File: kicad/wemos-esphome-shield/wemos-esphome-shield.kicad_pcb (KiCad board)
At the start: 2 copper layers, 74 x 52 mm, 28 parts, among them Q1 2N2219, Q2 2N2219, Q3 2N2219, T1 Transformer_1P_1S, U1 WeMos_D1_mini

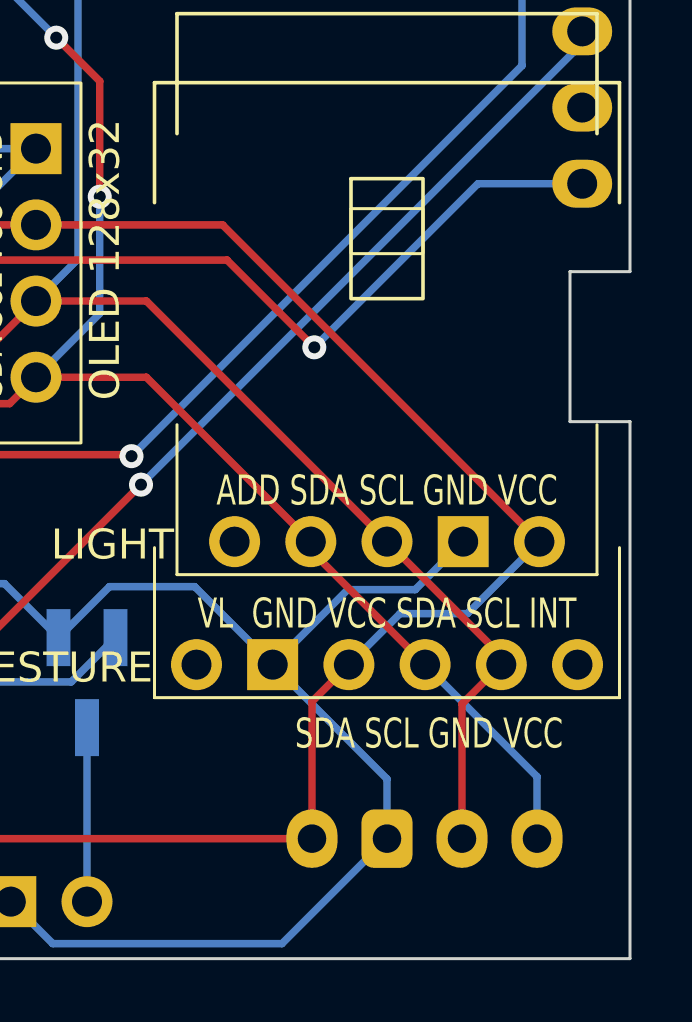
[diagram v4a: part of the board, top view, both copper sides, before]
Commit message: route gesture sensor to 3.3v power
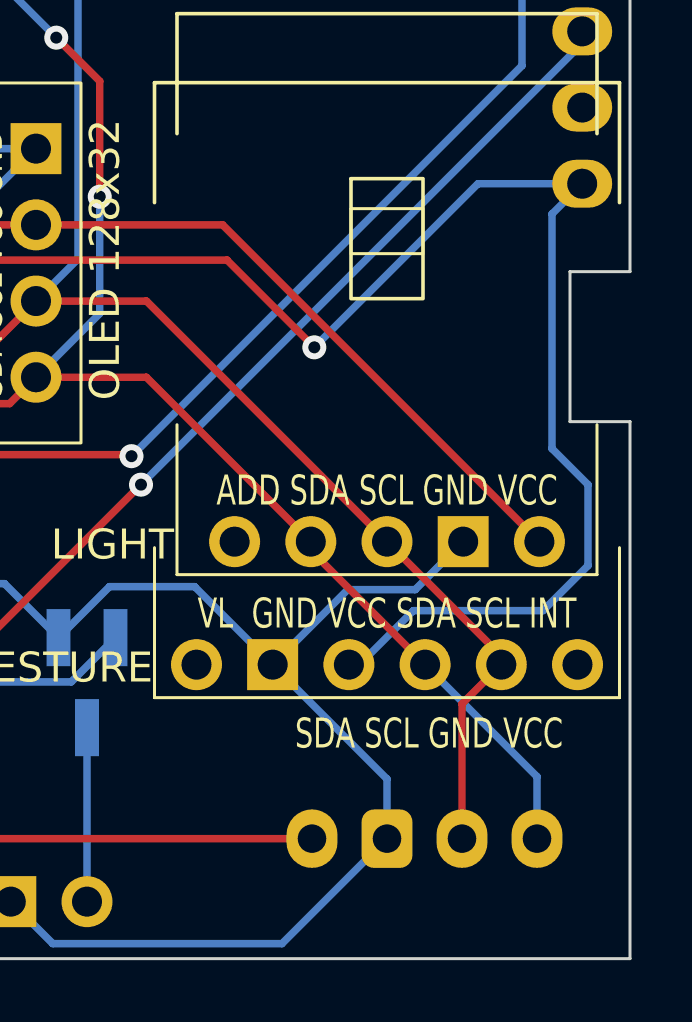
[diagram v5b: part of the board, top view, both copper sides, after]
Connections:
- GEST1 pad 3: 5V -> 3.3V
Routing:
- net 3.3V: track 79.0 -> 102.0 mm
- net 5V: track 219.6 -> 205.2 mm
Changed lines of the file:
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@@
       (net 6 "GND") (pinfunction "Pin_2") (pintype "passive"))
     (pad "3" thru_hole circle (at -1.27 0) (size 1.7 1.7) (drill 1) (layers "*.Cu" "*.Mask")
-      (net 1 "5V") (pinfunction "Pin_3") (pintype "passive"))
+      (net 5 "3.3V") (pinfunction "Pin_3") (pintype "passive"))
     (pad "4" thru_hole circle (at 1.27 0) (size 1.7 1.7) (drill 1) (layers "*.Cu" "*.Mask")
       (net 2 "SDA") (pinfunction "Pin_4") (pintype "passive"))
@@
   (segment (start 149.98 102.1) (end 139.42 91.54) (width 0.25) (layer "F.Cu") (net 1))
   (segment (start 117.17 101.4) (end 117.17 99.93) (width 0.25) (layer "F.Cu") (net 1))
-  (segment (start 142.4 112) (end 142.4 107.43) (width 0.25) (layer "F.Cu") (net 1))
   (segment (start 123.724 109.828) (end 107.924 109.828) (width 0.25) (layer "F.Cu") (net 1))
   (segment (start 123.724 109.828) (end 125.548 109.828) (width 0.25) (layer "F.Cu") (net 1))
@@
   (segment (start 112.7 88.2) (end 108.9 92) (width 0.25) (layer "F.Cu") (net 1))
   (segment (start 125.548 109.828) (end 129.82 114.1) (width 0.25) (layer "F.Cu") (net 1))
-  (segment (start 142.4 107.43) (end 143.63 106.2) (width 0.25) (layer "F.Cu") (net 1))
   (segment (start 83.712 104.748) (end 96.46 92) (width 0.25) (layer "F.Cu") (net 1))
   (segment (start 99.56 95.1) (end 123.4 95.1) (width 0.25) (layer "F.Cu") (net 1))
   (via (at 121 75.8) (size 0.8) (drill 0.4) (layers "F.Cu" "B.Cu") (net 1))
-  (segment (start 143.63 106.2) (end 145.33 104.5) (width 0.25) (layer "B.Cu") (net 1))
-  (segment (start 145.33 104.5) (end 147.58 104.5) (width 0.25) (layer "B.Cu") (net 1))
   (segment (start 121 72.51) (end 121 75.8) (width 0.25) (layer "B.Cu") (net 1))
-  (segment (start 147.58 104.5) (end 149.98 102.1) (width 0.25) (layer "B.Cu") (net 1))
   (segment (start 146.17 106.2) (end 142.36 102.39) (width 0.25) (layer "F.Cu") (net 2))
   (segment (start 80.838 112.368) (end 84 109.206) (width 0.25) (layer "F.Cu") (net 2))
@@
   (via (at 127.7 92.7) (size 0.8) (drill 0.4) (layers "F.Cu" "B.Cu") (net 5))
   (via (at 142.477347 95.622653) (size 0.8) (drill 0.4) (layers "F.Cu" "B.Cu") (net 5))
+  (segment (start 150.4 99) (end 150.4 91.177) (width 0.25) (layer "B.Cu") (net 5))
   (segment (start 112.732653 97.517347) (end 83.782653 97.517347) (width 0.25) (layer "B.Cu") (net 5))
   (segment (start 83.782653 97.517347) (end 80.838 100.462) (width 0.25) (layer "B.Cu") (net 5))
   (segment (start 127.7 92.7) (end 117.55 92.7) (width 0.25) (layer "B.Cu") (net 5))
   (segment (start 142.477347 95.622653) (end 147.93 90.17) (width 0.25) (layer "B.Cu") (net 5))
+  (segment (start 151.6 100.2) (end 150.4 99) (width 0.25) (layer "B.Cu") (net 5))
+  (segment (start 151.6 102.9) (end 151.6 100.2) (width 0.25) (layer "B.Cu") (net 5))
+  (segment (start 145.776396 104.4) (end 150.1 104.4) (width 0.25) (layer "B.Cu") (net 5))
   (segment (start 117.55 92.7) (end 112.732653 97.517347) (width 0.25) (layer "B.Cu") (net 5))
   (segment (start 80.838 100.462) (end 80.838 102.208) (width 0.25) (layer "B.Cu") (net 5))
+  (segment (start 150.4 91.177) (end 151.407 90.17) (width 0.25) (layer "B.Cu") (net 5))
+  (segment (start 150.1 104.4) (end 151.6 102.9) (width 0.25) (layer "B.Cu") (net 5))
+  (segment (start 143.63 106.2) (end 143.976396 106.2) (width 0.25) (layer "B.Cu") (net 5))
   (segment (start 147.93 90.17) (end 151.407 90.17) (width 0.25) (layer "B.Cu") (net 5))
+  (segment (start 143.976396 106.2) (end 145.776396 104.4) (width 0.25) (layer "B.Cu") (net 5))
   (segment (start 123.724 114.908) (end 126.132 112.5) (width 0.25) (layer "B.Cu") (net 6))
   (segment (start 129.75 103.5) (end 128.15 105.1) (width 0.25) (layer "B.Cu") (net 6))

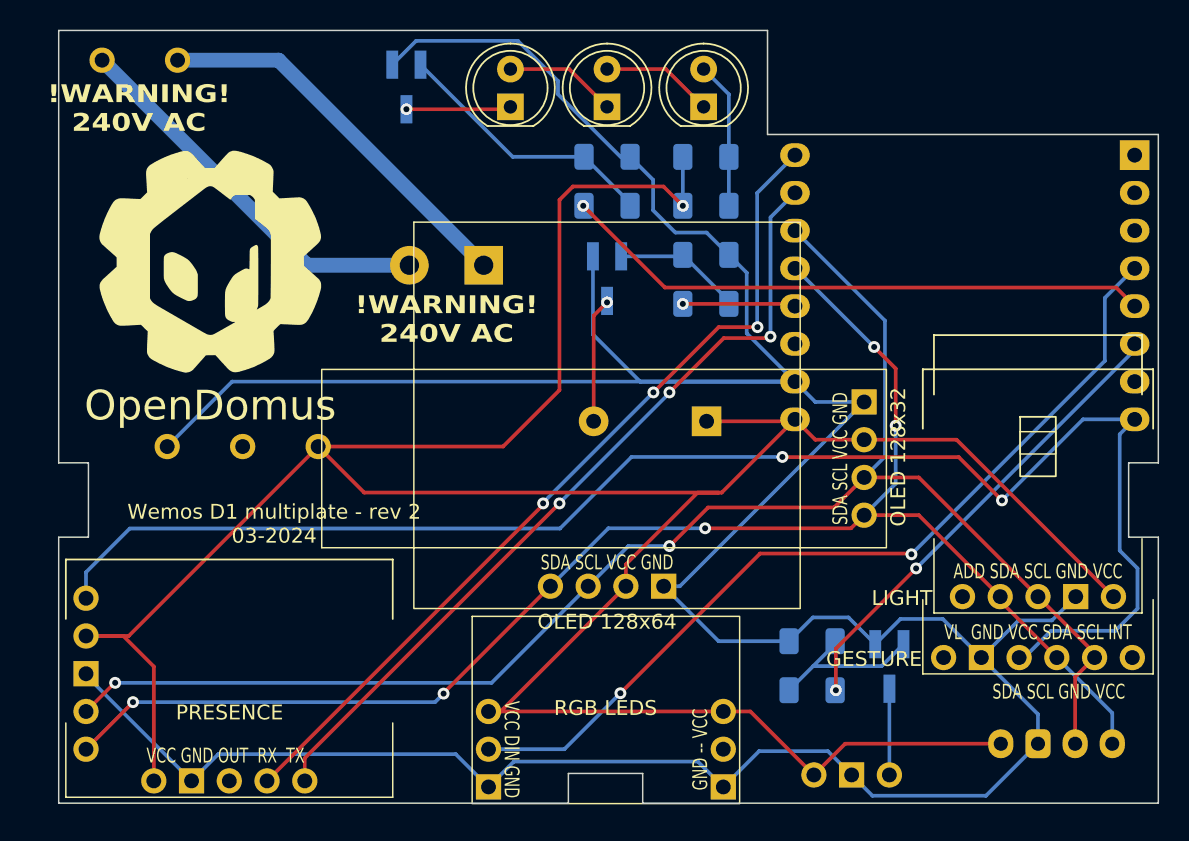
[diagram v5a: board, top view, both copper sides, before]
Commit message: custom SOT-23 footprint and other small adjustments
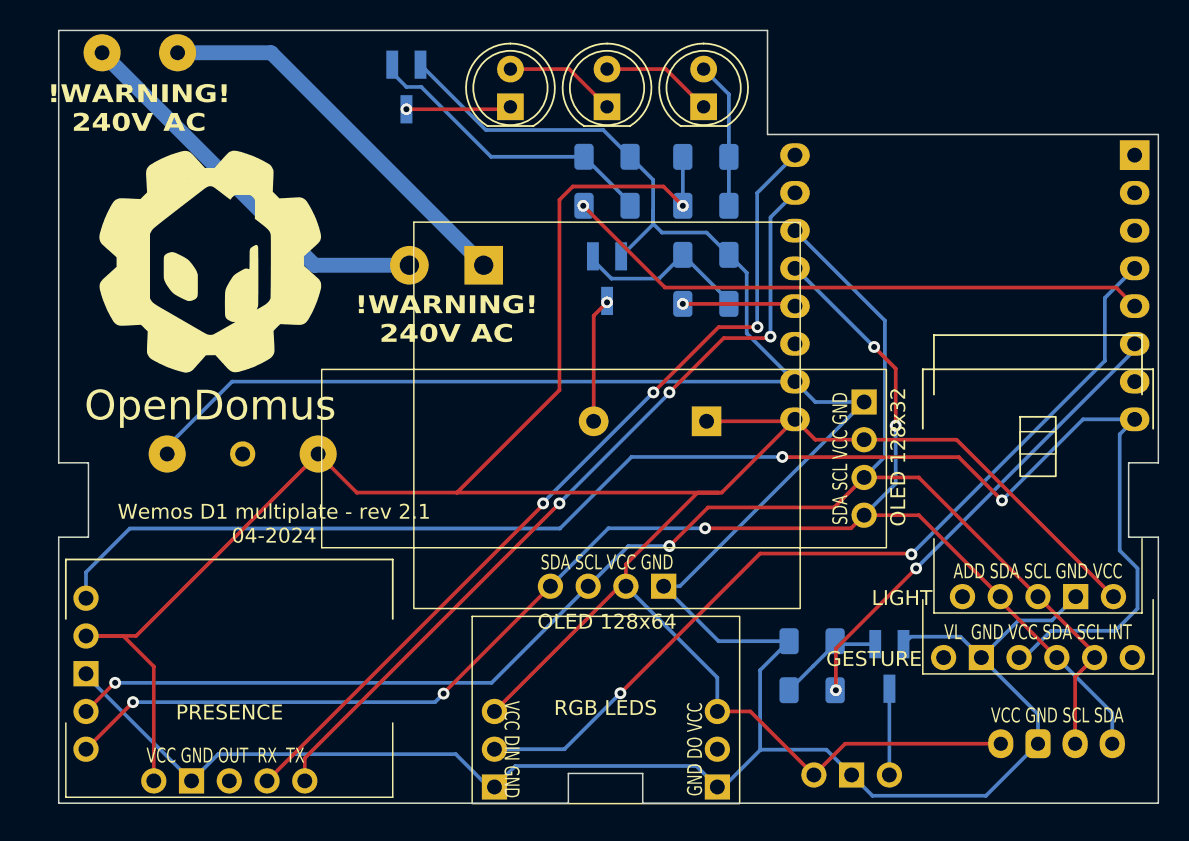
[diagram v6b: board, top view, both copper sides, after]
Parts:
- Q1, Q2, Q3: value 2N2219 -> 2N2222; footprint Package_TO_SOT_SMD:SOT-23_Handsoldering -> internal:SOT-23_Handsoldering
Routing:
- net GND: track 244.8 -> 222.9 mm
- net 5V: track 205.2 -> 192.7 mm
- net Net-(Q2-B): track 11.3 -> 7.37 mm
- net Net-(Q1-B): track 8.78 -> 12.1 mm
- net Net-(Q3-B): track 18.2 -> 20.4 mm
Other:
- board text added: "VCC GND SCL SDA"
- board text added: "Wemos D1 multiplate - rev 2.1 04-2024"
- board text removed: "SDA SCL GND VCC"
- board text removed: "Wemos D1 multiplate - rev 2 03-2024"

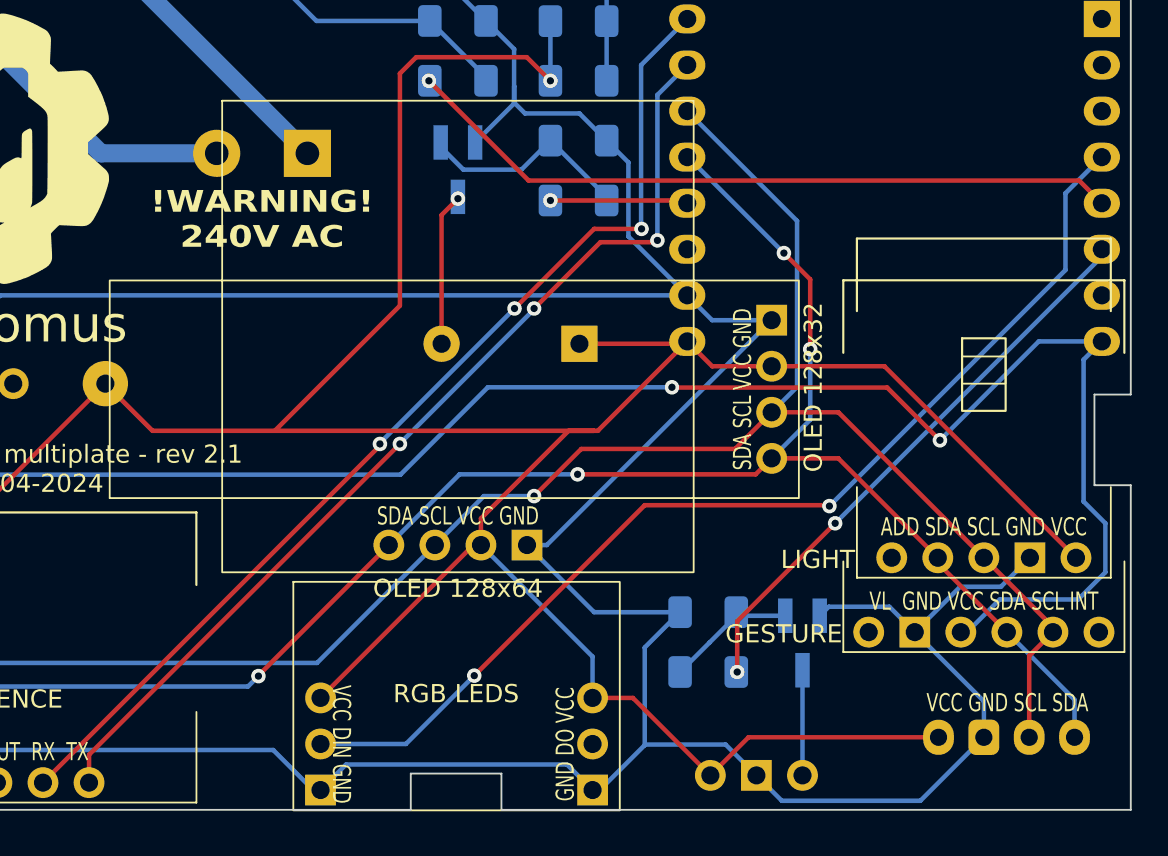
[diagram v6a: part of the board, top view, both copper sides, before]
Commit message: center oled display
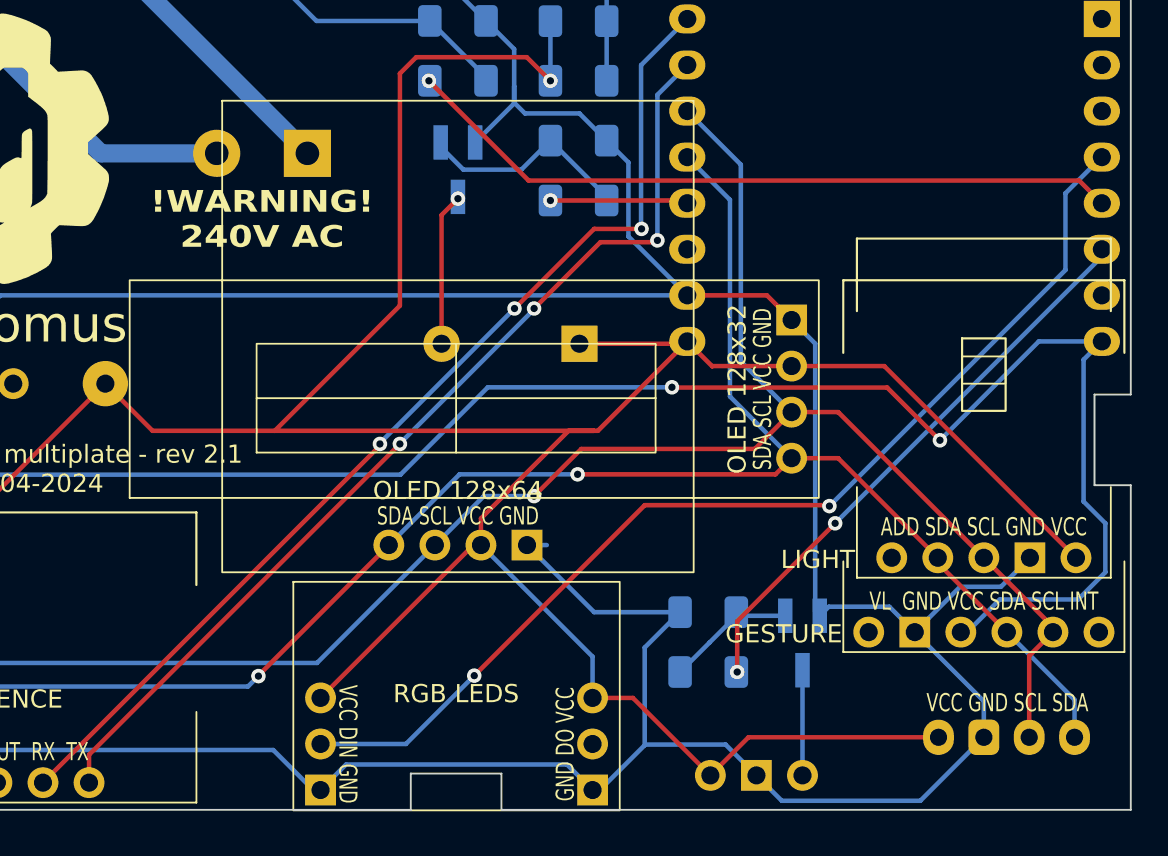
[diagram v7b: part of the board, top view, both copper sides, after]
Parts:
- moved OLED1 1.10 mm to (134.3, 92.8)
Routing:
- net SDA: track 103.7 -> 102.4 mm, vias 5 -> 3
- net SCL: track 105.6 -> 104.9 mm
- net GND: track 222.9 -> 223.4 mm

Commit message: reroute buzzer to D8
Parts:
- turned R1 to 180 degrees
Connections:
- R1 pad 1: D3 -> D8
- U1 pad 12: D3 -> unconnected-(U1-D3-Pad12)
- U1 pad 7: unconnected-(U1-CS/D8-Pad7) -> D8
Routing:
- net D8: track 0.00 -> 29.7 mm, vias 0 -> 1
- net D3: track 7.61 -> 0.00 mm, vias 1 -> 0
- net Net-(Q1-B): track 12.1 -> 10.8 mm
- net GND: track 223.4 -> 222.3 mm
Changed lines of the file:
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@@
   (net 7 "Net-(BZ1--)")
   (net 8 "D5")
-  (net 9 "D3")
+  (net 9 "D8")
   (net 10 "L")
   (net 11 "N")
@@
   (net 29 "unconnected-(U1-A0-Pad2)")
   (net 30 "unconnected-(U1-D0-Pad3)")
-  (net 31 "unconnected-(U1-CS{slash}D8-Pad7)")
+  (net 31 "unconnected-(U1-D3-Pad12)")
   (net 32 "unconnected-(U1-D4-Pad11)")
   (footprint "LED_THT:LED_D5.0mm" (layer "F.Cu")
@@
   )
   (footprint "Resistor_SMD:R_1206_3216Metric_Pad1.30x1.75mm_HandSolder" (layer "B.Cu")
-    (at 122.55 82.4)
+    (at 122.55 82.4 180)
     (descr "Resistor SMD 1206 (3216 Metric), square (rectangular) end terminal, IPC_7351 nominal with elongated pad for handsoldering. (Body size source: IPC-SM-782 page 72, https://www.pcb-3d.com/wordpress/wp-content/uploads/ipc-sm-782a_amendment_1_and_2.pdf), generated with kicad-footprint-generator")
     (tags "resistor handsolder")
@@
     (fp_line (start 1.6 0.8) (end 1.6 -0.8)
       (stroke (width 0.1) (type solid)) (layer "B.Fab"))
-    (pad "1" smd roundrect (at -1.55 0) (size 1.3 1.75) (layers "B.Cu" "B.Paste" "B.Mask") (roundrect_rratio 0.1923076923)
-      (net 9 "D3") (pintype "passive"))
-    (pad "2" smd roundrect (at 1.55 0) (size 1.3 1.75) (layers "B.Cu" "B.Paste" "B.Mask") (roundrect_rratio 0.1923076923)
+    (pad "1" smd roundrect (at -1.55 0 180) (size 1.3 1.75) (layers "B.Cu" "B.Paste" "B.Mask") (roundrect_rratio 0.1923076923)
+      (net 9 "D8") (pintype "passive"))
+    (pad "2" smd roundrect (at 1.55 0 180) (size 1.3 1.75) (layers "B.Cu" "B.Paste" "B.Mask") (roundrect_rratio 0.1923076923)
       (net 24 "Net-(Q1-B)") (pintype "passive"))
     (model "${KICAD6_3DMODEL_DIR}/Resistor_SMD.3dshapes/R_1206_3216Metric.wrl"
@@
       (net 12 "D7") (pinfunction "MOSI/D7") (pintype "bidirectional"))
     (pad "7" thru_hole oval (at 0 -15.24 180) (size 2 1.6) (drill 1) (layers "*.Cu" "*.Mask")
-      (net 31 "unconnected-(U1-CS{slash}D8-Pad7)") (pinfunction "CS/D8") (pintype "bidirectional+no_connect"))
+      (net 9 "D8") (pinfunction "CS/D8") (pintype "bidirectional"))
     (pad "8" thru_hole oval (at 0 -17.78 180) (size 2 1.6) (drill 1) (layers "*.Cu" "*.Mask")
       (net 5 "3.3V") (pinfunction "3V3") (pintype "power_out"))
@@
       (net 32 "unconnected-(U1-D4-Pad11)") (pinfunction "D4") (pintype "bidirectional+no_connect"))
     (pad "12" thru_hole oval (at 22.86 -10.16 180) (size 2 1.6) (drill 1) (layers "*.Cu" "*.Mask")
-      (net 9 "D3") (pinfunction "D3") (pintype "bidirectional"))
+      (net 31 "unconnected-(U1-D3-Pad12)") (pinfunction "D3") (pintype "bidirectional+no_connect"))
     (pad "13" thru_hole oval (at 22.86 -7.62 180) (size 2 1.6) (drill 1) (layers "*.Cu" "*.Mask")
       (net 2 "SDA") (pinfunction "SDA/D2") (pintype "bidirectional"))
@@
   (segment (start 130.66 112.4) (end 126.232 112.4) (width 0.25) (layer "B.Cu") (net 6))
   (segment (start 119 77) (end 119.6 77.6) (width 0.25) (layer "B.Cu") (net 6))
-  (segment (start 119.71 101.4) (end 120.8 101.4) (width 0.25) (layer "B.Cu") (net 6))
   (segment (start 126.232 112.4) (end 126.2 112.432) (width 0.25) (layer "B.Cu") (net 6))
   (segment (start 135.85 105.3) (end 136.35 104.8) (width 0.25) (layer "B.Cu") (net 6))
@@
   (segment (start 151.39 80.01) (end 151.407 80.01) (width 0.25) (layer "B.Cu") (net 8))
   (segment (start 149.4 86.235087) (end 149.4 82) (width 0.25) (layer "B.Cu") (net 8))
-  (segment (start 121 82.4) (end 128.397 82.4) (width 0.25) (layer "F.Cu") (net 9))
-  (segment (start 128.397 82.4) (end 128.547 82.55) (width 0.25) (layer "F.Cu") (net 9))
-  (via (at 121 82.4) (size 0.8) (drill 0.4) (layers "F.Cu" "B.Cu") (net 9))
+  (segment (start 124.1 82.4) (end 126.2 82.4) (width 0.25) (layer "F.Cu") (net 9))
+  (segment (start 126.2 82.4) (end 127.6 83.8) (width 0.25) (layer "F.Cu") (net 9))
+  (segment (start 127.6 83.8) (end 147.577 83.8) (width 0.25) (layer "F.Cu") (net 9))
+  (segment (start 147.577 83.8) (end 151.407 87.63) (width 0.25) (layer "F.Cu") (net 9))
+  (via (at 124.1 82.4) (size 0.8) (drill 0.4) (layers "F.Cu" "B.Cu") (net 9))
+  (segment (start 124.1 82.4) (end 124.1 82.2) (width 0.25) (layer "B.Cu") (net 9))
   (segment (start 96.22 79.8) (end 102.6 79.8) (width 1) (layer "B.Cu") (net 10))
   (segment (start 81.92 65.5) (end 96.22 79.8) (width 1) (layer "B.Cu") (net 10))
@@
   (segment (start 114.95 79.45) (end 116.2 80.7) (width 0.25) (layer "B.Cu") (net 24))
   (segment (start 119.4 80.7) (end 121 79.1) (width 0.25) (layer "B.Cu") (net 24))
-  (segment (start 124.1 82.2) (end 121 79.1) (width 0.25) (layer "B.Cu") (net 24))
   (segment (start 114.95 79.2) (end 114.95 79.45) (width 0.25) (layer "B.Cu") (net 24))
+  (segment (start 121 79.1) (end 121 82.4) (width 0.25) (layer "B.Cu") (net 24))
   (segment (start 116.2 80.7) (end 119.4 80.7) (width 0.25) (layer "B.Cu") (net 24))
-  (segment (start 124.1 82.4) (end 124.1 82.2) (width 0.25) (layer "B.Cu") (net 24))
   (segment (start 129.775 106.775) (end 128.15 108.4) (width 0.25) (layer "B.Cu") (net 25))
   (segment (start 131.45 105.3) (end 131.25 105.1) (width 0.25) (layer "B.Cu") (net 25))
@@
   (segment (start 108.1 72.5) (end 114.35 72.5) (width 0.25) (layer "B.Cu") (net 27))
   (segment (start 102.4 67.8) (end 103.4 67.8) (width 0.25) (layer "B.Cu") (net 27))
+  (segment (start 128.397 82.4) (end 128.547 82.55) (width 0.25) (layer "F.Cu") (net 31))
   (group "" (id 177400ad-17ae-4b70-9624-3276b1606058)
     (members
